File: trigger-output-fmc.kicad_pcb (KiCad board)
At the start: 8 copper layers, 84 x 69 mm, 346 parts, among them J1 MMCX, J10 MMCX, J11 MMCX, J12 MMCX, J13 MMCX, J14 MMCX, J15 MMCX, J16 MMCX, J19 WP Jumper, J2 MMCX, J3 MMCX, J4 MMCX, J5 MMCX, J6 MMCX, J7 MMCX, J8 MMCX, J9 MMCX, P1 ASP-134488-01, Q1 FDN335N, Q2 FDN335N, Q3 FDN335N, T1 TCM2-43X+, T2 TCM2-43X+, T3 TCM2-43X+, T4 TCM2-43X+, U1 TLV3601, U10 SN74LVC2G126, U11 TLV3601, U12 SN74LVC2G126, U13 TLV3601, U14 SN74LVC2G126, U15 TLV3601, U16 SN74LVC2G126, U17 TLV3601, U18 SI5394, U19 SI5394, U2 TLV3601, U20 TLV75733PDBV, U21 TLV75718PDBV, U22 TPS563200, U23 74AVC4T245, U24 TLV75733PDBV, U25 74AVC4T245, U26 74LVC8T245, U27 74LVC8T245, U28 TLV75718PDBV, U29 SN74LVC2G126, U3 TLV3601, U30 TLV3601, U31 SN74LVC2G126, U32 TLV3601, U33 SN74LVC2G126, U34 TLV3601, U35 SN74LVC2G126, U36 TLV3601, U37 SN74LVC2G126, U38 TLV3601, U39 SN74LVC2G126, U4 SN74LVC2G126, U40 TLV3601, U41 SN74LVC2G126, U42 TLV3601, U43 SN74LVC2G126, U44 LP3855EMP-ADJ/NOPB, U48 SN74LVC2G126, U5 SN74LVC2G126, U6 TLV3601, U7 SN74LVC2G126, U8 TLV3601, U9 AT24C64D, Y1 CX3225SB48000D0FPJC1, Y2 CX3225SB48000D0FPJC1

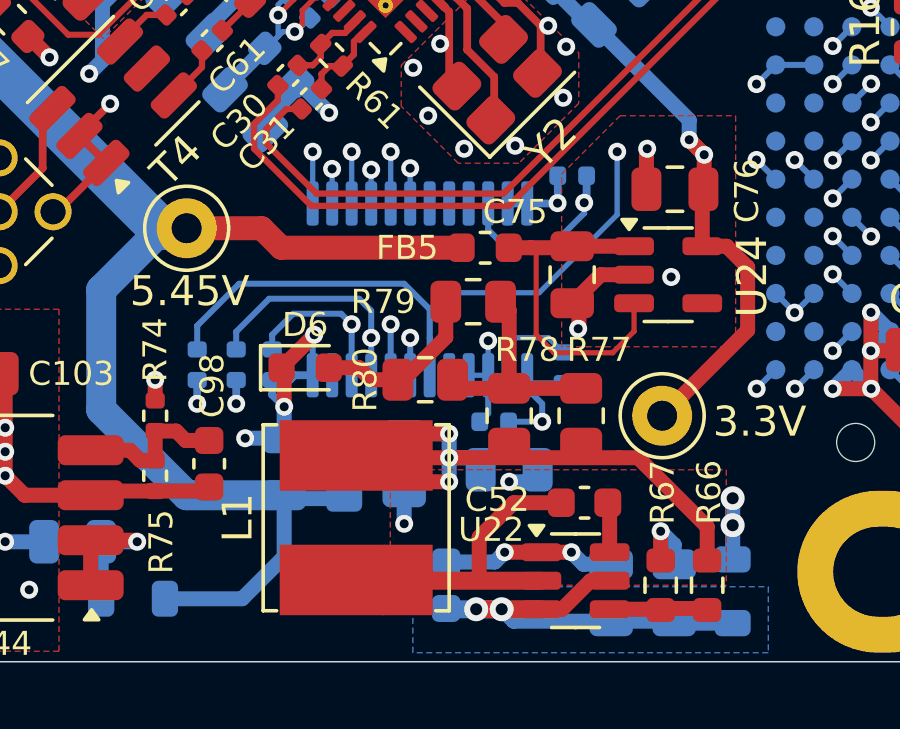
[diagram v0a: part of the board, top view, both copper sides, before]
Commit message: Revert "Added 50mA load with LED"
This reverts commit e684fa44ce82bf8659985c78fe183713544e1072.
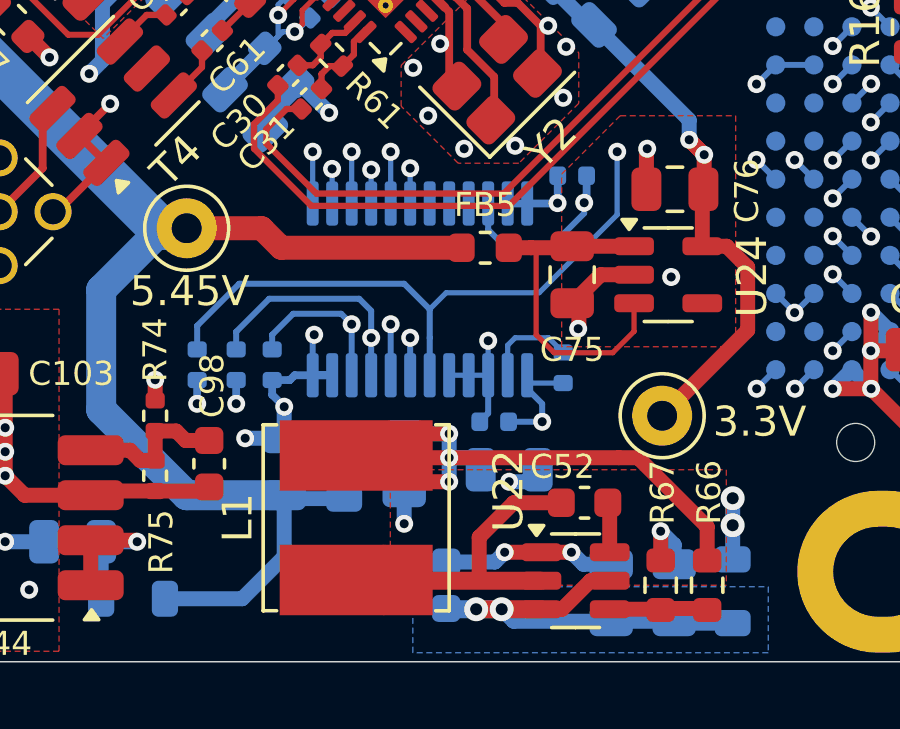
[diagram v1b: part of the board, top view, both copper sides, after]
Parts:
- removed D6: Green, LED_SMD:LED_0603_1608Metric
- removed R77, R78, R79, R80: 88.7R, Resistor_SMD:R_0805_2012Metric
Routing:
- net Net-(R77-Pad1): track 7.41 -> 0.00 mm
- net Net-(D6-A): track 5.84 -> 0.00 mm
- net GND: track 521.5 -> 518.6 mm
